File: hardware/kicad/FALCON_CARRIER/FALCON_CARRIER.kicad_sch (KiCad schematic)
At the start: 49 parts, among them J1 POWER_INPUT, J10 LEAK_SENSOR_TBD, J11 FAN1_MOLEX_470531000, J12 SERVICE_I2C, J13 FAN2_MOLEX_470531000, J2 BAR02_I2C, J3 GPS_UART, J4 INA260_BAT_LOGIC, J5 INA260_SOLAR_0X41, J6 MCP9808_0X18, J7 ANEMOMETER, J8 WIND_VANE, J9 DS18B20_OPTION, Q1 2N7002_FAN1_PWM, Q2 2N7002_FAN2_PWM, U1 REGULATOR_3V3_TBD, U2 ESP32_DEVKITC_V4_WROOM32E, U3 BNO085_SPI, U4 ADS1115_0X48, U6 EFUSE_TPS25947_TBD

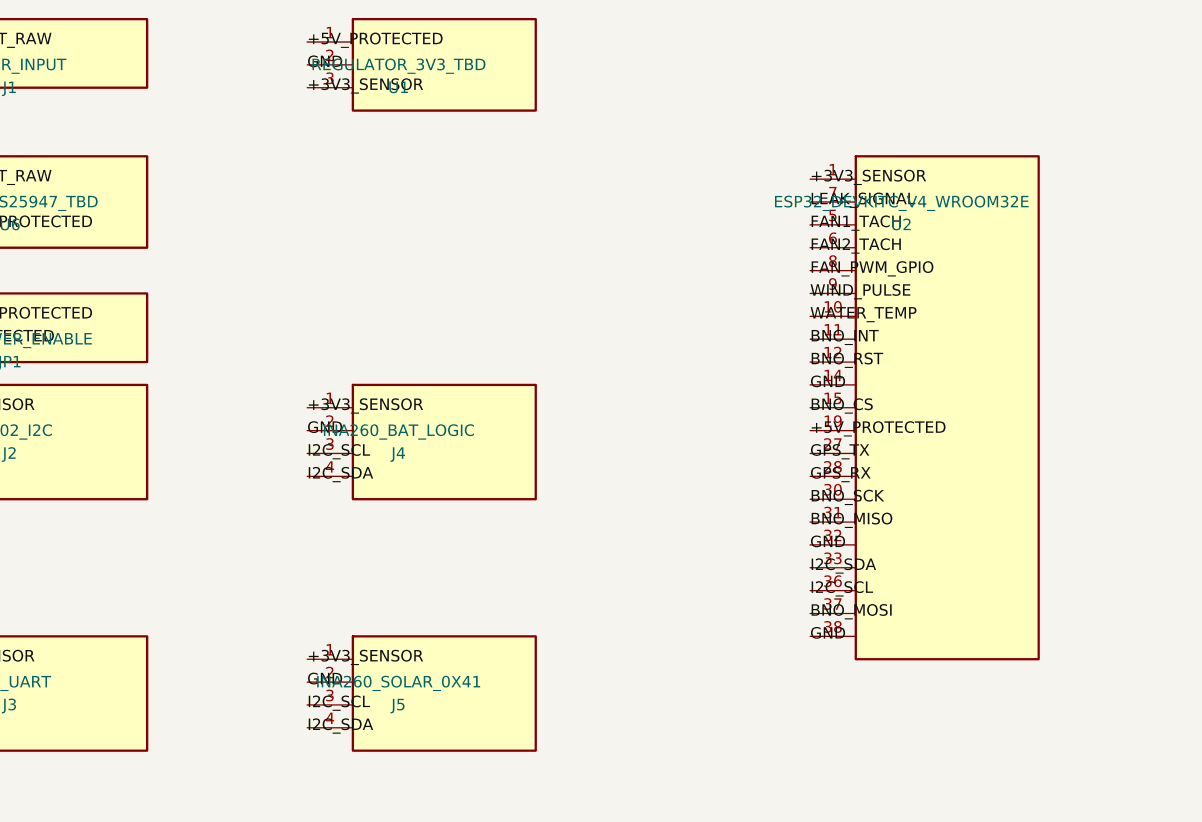
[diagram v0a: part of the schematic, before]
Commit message: Implement dedicated 3V3 sensor regulator
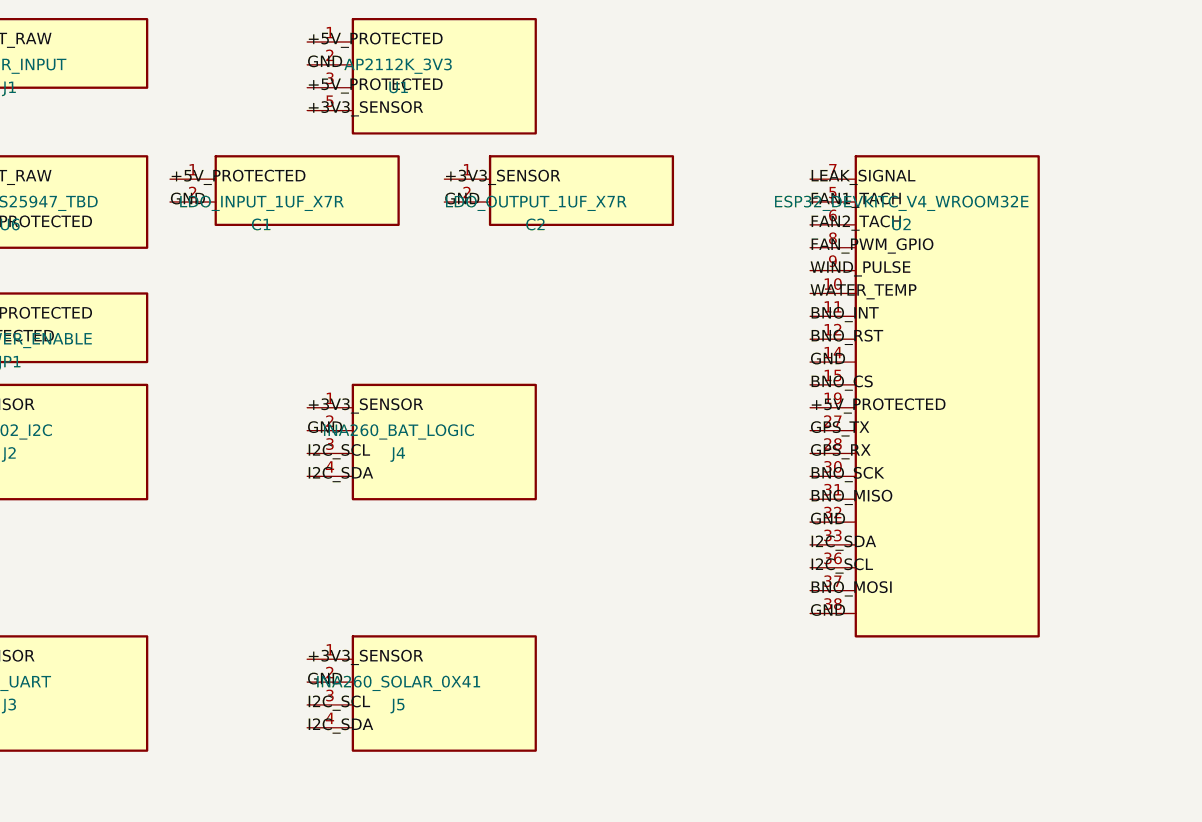
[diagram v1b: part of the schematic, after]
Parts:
- added C1: LDO_INPUT_1UF_X7R, symbol FALCON:LDO_INPUT_1UF_X7R
- added C2: LDO_OUTPUT_1UF_X7R, symbol FALCON:LDO_OUTPUT_1UF_X7R
- U1: value REGULATOR_3V3_TBD -> AP2112K_3V3; symbol FALCON:REGULATOR_3V3_TBD -> FALCON:AP2112K_3V3
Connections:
- net +3V3_SENSOR: now also U1.5 (+3V3_SENSOR), C2.1 (+3V3_SENSOR); no longer U1.3 (+3V3_SENSOR), U2.1 (+3V3_SENSOR)
- net +5V_PROTECTED: now also U1.3 (+5V_PROTECTED), C1.1 (+5V_PROTECTED)
- net GND: now also C1.2 (GND), C2.2 (GND)
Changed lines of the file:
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@@
   (label "GND" (at 88.90 38.10 0)
     (effects (font (size 1.27 1.27))))
-  (label "+3V3_SENSOR" (at 88.90 40.64 0)
-    (effects (font (size 1.27 1.27))))
-  (label "+3V3_SENSOR" (at 144.78 50.80 0)
-    (effects (font (size 1.27 1.27))))
-  (label "LEAK_SIGNAL" (at 144.78 53.34 0)
-    (effects (font (size 1.27 1.27))))
-  (label "FAN1_TACH" (at 144.78 55.88 0)
-    (effects (font (size 1.27 1.27))))
-  (label "FAN2_TACH" (at 144.78 58.42 0)
-    (effects (font (size 1.27 1.27))))
-  (label "FAN_PWM_GPIO" (at 144.78 60.96 0)
-    (effects (font (size 1.27 1.27))))
-  (label "WIND_PULSE" (at 144.78 63.50 0)
-    (effects (font (size 1.27 1.27))))
-  (label "WATER_TEMP" (at 144.78 66.04 0)
-    (effects (font (size 1.27 1.27))))
-  (label "BNO_INT" (at 144.78 68.58 0)
-    (effects (font (size 1.27 1.27))))
-  (label "BNO_RST" (at 144.78 71.12 0)
-    (effects (font (size 1.27 1.27))))
-  (label "GND" (at 144.78 73.66 0)
-    (effects (font (size 1.27 1.27))))
-  (label "BNO_CS" (at 144.78 76.20 0)
-    (effects (font (size 1.27 1.27))))
-  (label "+5V_PROTECTED" (at 144.78 78.74 0)
-    (effects (font (size 1.27 1.27))))
-  (label "GPS_TX" (at 144.78 81.28 0)
-    (effects (font (size 1.27 1.27))))
-  (label "GPS_RX" (at 144.78 83.82 0)
-    (effects (font (size 1.27 1.27))))
-  (label "BNO_SCK" (at 144.78 86.36 0)
-    (effects (font (size 1.27 1.27))))
-  (label "BNO_MISO" (at 144.78 88.90 0)
-    (effects (font (size 1.27 1.27))))
-  (label "GND" (at 144.78 91.44 0)
-    (effects (font (size 1.27 1.27))))
-  (label "I2C_SDA" (at 144.78 93.98 0)
-    (effects (font (size 1.27 1.27))))
-  (label "I2C_SCL" (at 144.78 96.52 0)
-    (effects (font (size 1.27 1.27))))
-  (label "BNO_MOSI" (at 144.78 99.06 0)
-    (effects (font (size 1.27 1.27))))
-  (label "GND" (at 144.78 101.60 0)
+  (label "+5V_PROTECTED" (at 88.90 40.64 0)
+    (effects (font (size 1.27 1.27))))
+  (label "+3V3_SENSOR" (at 88.90 43.18 0)
+    (effects (font (size 1.27 1.27))))
+  (label "+5V_PROTECTED" (at 73.66 50.80 0)
+    (effects (font (size 1.27 1.27))))
+  (label "GND" (at 73.66 53.34 0)
+    (effects (font (size 1.27 1.27))))
+  (label "+3V3_SENSOR" (at 104.14 50.80 0)
+    (effects (font (size 1.27 1.27))))
+  (label "GND" (at 104.14 53.34 0)
+    (effects (font (size 1.27 1.27))))
+  (label "LEAK_SIGNAL" (at 144.78 50.80 0)
+    (effects (font (size 1.27 1.27))))
+  (label "FAN1_TACH" (at 144.78 53.34 0)
+    (effects (font (size 1.27 1.27))))
+  (label "FAN2_TACH" (at 144.78 55.88 0)
+    (effects (font (size 1.27 1.27))))
+  (label "FAN_PWM_GPIO" (at 144.78 58.42 0)
+    (effects (font (size 1.27 1.27))))
+  (label "WIND_PULSE" (at 144.78 60.96 0)
+    (effects (font (size 1.27 1.27))))
+  (label "WATER_TEMP" (at 144.78 63.50 0)
+    (effects (font (size 1.27 1.27))))
+  (label "BNO_INT" (at 144.78 66.04 0)
+    (effects (font (size 1.27 1.27))))
+  (label "BNO_RST" (at 144.78 68.58 0)
+    (effects (font (size 1.27 1.27))))
+  (label "GND" (at 144.78 71.12 0)
+    (effects (font (size 1.27 1.27))))
+  (label "BNO_CS" (at 144.78 73.66 0)
+    (effects (font (size 1.27 1.27))))
+  (label "+5V_PROTECTED" (at 144.78 76.20 0)
+    (effects (font (size 1.27 1.27))))
+  (label "GPS_TX" (at 144.78 78.74 0)
+    (effects (font (size 1.27 1.27))))
+  (label "GPS_RX" (at 144.78 81.28 0)
+    (effects (font (size 1.27 1.27))))
+  (label "BNO_SCK" (at 144.78 83.82 0)
+    (effects (font (size 1.27 1.27))))
+  (label "BNO_MISO" (at 144.78 86.36 0)
+    (effects (font (size 1.27 1.27))))
+  (label "GND" (at 144.78 88.90 0)
+    (effects (font (size 1.27 1.27))))
+  (label "I2C_SDA" (at 144.78 91.44 0)
+    (effects (font (size 1.27 1.27))))
+  (label "I2C_SCL" (at 144.78 93.98 0)
+    (effects (font (size 1.27 1.27))))
+  (label "BNO_MOSI" (at 144.78 96.52 0)
+    (effects (font (size 1.27 1.27))))
+  (label "GND" (at 144.78 99.06 0)
     (effects (font (size 1.27 1.27))))
   (label "+3V3_SENSOR" (at 210.82 45.72 0)
@@
   )
   (symbol
-    (lib_id "FALCON:REGULATOR_3V3_TBD") (at 99.06 35.56 0) (unit 1)
+    (lib_id "FALCON:AP2112K_3V3") (at 99.06 35.56 0) (unit 1)
     (exclude_from_sim no) (in_bom yes) (on_board yes) (dnp no)
     (property "Reference" "U1" (at 99.06 40.64 0) (effects (font (size 1.27 1.27))))
-    (property "Value" "REGULATOR_3V3_TBD" (at 99.06 38.10 0) (effects (font (size 1.27 1.27))))
+    (property "Value" "AP2112K_3V3" (at 99.06 38.10 0) (effects (font (size 1.27 1.27))))
     (property "Footprint" "" (at 99.06 35.56 0) (effects (font (size 1.27 1.27)) (hide yes)))
     (property "Datasheet" "" (at 99.06 35.56 0) (effects (font (size 1.27 1.27)) (hide yes)))
@@
     (pin "2")
     (pin "3")
+    (pin "5")
     (instances (project "FALCON_CARRIER"
       (path "/8f84bda8-4a60-4fb6-9df1-43d0356dc759" (reference "U1") (unit 1))))
+  )
+  (symbol
+    (lib_id "FALCON:LDO_INPUT_1UF_X7R") (at 83.82 50.80 0) (unit 1)
+    (exclude_from_sim no) (in_bom yes) (on_board yes) (dnp no)
+    (property "Reference" "C1" (at 83.82 55.88 0) (effects (font (size 1.27 1.27))))
+    (property "Value" "LDO_INPUT_1UF_X7R" (at 83.82 53.34 0) (effects (font (size 1.27 1.27))))
+    (property "Footprint" "" (at 83.82 50.80 0) (effects (font (size 1.27 1.27)) (hide yes)))
+    (property "Datasheet" "" (at 83.82 50.80 0) (effects (font (size 1.27 1.27)) (hide yes)))
+    (property "Description" "FALCON carrier placeholder; footprint TBD" (at 83.82 50.80 0) (effects (font (size 1.27 1.27)) (hide yes)))
+    (pin "1")
+    (pin "2")
+    (instances (project "FALCON_CARRIER"
+      (path "/8f84bda8-4a60-4fb6-9df1-43d0356dc759" (reference "C1") (unit 1))))
+  )
+  (symbol
+    (lib_id "FALCON:LDO_OUTPUT_1UF_X7R") (at 114.30 50.80 0) (unit 1)
+    (exclude_from_sim no) (in_bom yes) (on_board yes) (dnp no)
+    (property "Reference" "C2" (at 114.30 55.88 0) (effects (font (size 1.27 1.27))))
+    (property "Value" "LDO_OUTPUT_1UF_X7R" (at 114.30 53.34 0) (effects (font (size 1.27 1.27))))
+    (property "Footprint" "" (at 114.30 50.80 0) (effects (font (size 1.27 1.27)) (hide yes)))
+    (property "Datasheet" "" (at 114.30 50.80 0) (effects (font (size 1.27 1.27)) (hide yes)))
+    (property "Description" "FALCON carrier placeholder; footprint TBD" (at 114.30 50.80 0) (effects (font (size 1.27 1.27)) (hide yes)))
+    (pin "1")
+    (pin "2")
+    (instances (project "FALCON_CARRIER"
+      (path "/8f84bda8-4a60-4fb6-9df1-43d0356dc759" (reference "C2") (unit 1))))
   )
   (symbol
@@
     (property "Datasheet" "" (at 154.94 50.80 0) (effects (font (size 1.27 1.27)) (hide yes)))
     (property "Description" "FALCON carrier placeholder; footprint TBD" (at 154.94 50.80 0) (effects (font (size 1.27 1.27)) (hide yes)))
-    (pin "1")
     (pin "7")
     (pin "5")

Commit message: Redesign FALCON carrier schematic blocks
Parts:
- removed C1: LDO_INPUT_1UF_X7R, symbol FALCON:LDO_INPUT_1UF_X7R
- removed C2: LDO_OUTPUT_1UF_X7R, symbol FALCON:LDO_OUTPUT_1UF_X7R
- removed J1: POWER_INPUT, symbol FALCON:POWER_INPUT
- removed J10: LEAK_SENSOR_TBD, symbol FALCON:LEAK_SENSOR_TBD
- removed J11: FAN1_MOLEX_470531000, symbol FALCON:FAN1_MOLEX_470531000
- removed J12: SERVICE_I2C, symbol FALCON:SERVICE_I2C
- removed J13: FAN2_MOLEX_470531000, symbol FALCON:FAN2_MOLEX_470531000
- removed J2: BAR02_I2C, symbol FALCON:BAR02_I2C
- removed J3: GPS_UART, symbol FALCON:GPS_UART
- removed J4: INA260_BAT_LOGIC, symbol FALCON:INA260_BAT_LOGIC
- removed J5: INA260_SOLAR_0X41, symbol FALCON:INA260_SOLAR_0X41
- removed J6: MCP9808_0X18, symbol FALCON:MCP9808_0X18
- removed J7: ANEMOMETER, symbol FALCON:ANEMOMETER
- removed J8: WIND_VANE, symbol FALCON:WIND_VANE
- removed J9: DS18B20_OPTION, symbol FALCON:DS18B20_OPTION
- removed JP1: EXT_POWER_ENABLE, symbol FALCON:EXT_POWER_ENABLE
- removed Q1: 2N7002_FAN1_PWM, symbol FALCON:2N7002_FAN1_PWM
- removed Q2: 2N7002_FAN2_PWM, symbol FALCON:2N7002_FAN2_PWM
- removed R1: PULLUP_10K, symbol FALCON:PULLUP_10K
- removed R2: PULLUP_4K7, symbol FALCON:PULLUP_4K7
- removed R3: FAN1_GATE_100R, symbol FALCON:FAN1_GATE_100R
- removed R4: FAN2_GATE_100R, symbol FALCON:FAN2_GATE_100R
- removed R5: FAN1_GATE_PULLDOWN_100K, symbol FALCON:FAN1_GATE_PULLDOWN_100K
- removed R6: FAN2_GATE_PULLDOWN_100K, symbol FALCON:FAN2_GATE_PULLDOWN_100K
- removed R7: FAN1_TACH_PULLUP_10K, symbol FALCON:FAN1_TACH_PULLUP_10K
- removed R8: FAN2_TACH_PULLUP_10K, symbol FALCON:FAN2_TACH_PULLUP_10K
- removed TP1, TP10, TP11, TP12, TP13, TP14, TP15, TP16, TP17, TP18, TP19, TP2, TP20, TP3, TP4, TP5, TP6, TP7, TP8, TP9: TEST_POINT, symbol FALCON:TEST_POINT
- removed U3: BNO085_SPI, symbol FALCON:BNO085_SPI
- removed U4: ADS1115_0X48, symbol FALCON:ADS1115_0X48
- removed U6: EFUSE_TPS25947_TBD, symbol FALCON:EFUSE_TPS25947_TBD
- added C1: 1UF_LDO_IN, Capacitor_SMD:C_0603_1608Metric, symbol FALCON:1UF_LDO_IN
- added C2: 1UF_LDO_OUT, Capacitor_SMD:C_0603_1608Metric, symbol FALCON:1UF_LDO_OUT
- added C3: 10UF_25V_INPUT, Capacitor_SMD:C_0603_1608Metric, symbol FALCON:10UF_25V_INPUT
- added C4: 47UF_10V_OUTPUT, Capacitor_SMD:C_1210_3225Metric, symbol FALCON:47UF_10V_OUTPUT
- added C5: 100NF_5V_DECOUPLING, Capacitor_SMD:C_0603_1608Metric, symbol FALCON:100NF_5V_DECOUPLING
- added C6: 10UF_5V_BULK, Capacitor_SMD:C_0805_2012Metric, symbol FALCON:10UF_5V_BULK
- added D1: SMBJ18A_TVS, Diode_SMD:D_SMA, symbol FALCON:SMBJ18A_TVS
- added D2: 5V_POWER_LED, LED_SMD:LED_0603_1608Metric, symbol FALCON:5V_POWER_LED
- added D3: 3V3_POWER_LED, LED_SMD:LED_0603_1608Metric, symbol FALCON:3V3_POWER_LED
- added D4: STATUS_LED, LED_SMD:LED_0603_1608Metric, symbol FALCON:STATUS_LED
- added F1: FUSE_3A_DC_TBD, Fuse:Fuse_1206_3216Metric, symbol FALCON:FUSE_3A_DC_TBD
- added F2: USB_POLYFUSE_1A, Fuse:Fuse_1206_3216Metric, symbol FALCON:USB_POLYFUSE_1A
- added J10: LEAK_SENSOR_INTERFACE, Connector_PinHeader_2.54mm:PinHeader_1x03_P2.54mm_Vertical, symbol FALCON:LEAK_SENSOR_INTERFACE
- added J14: SOLAR_INPUT_TO_EXTERNAL_MPPT, Connector_JST:JST_VH_B2P-VH-B_1x02_P3.96mm_Vertical, symbol FALCON:SOLAR_INPUT_TO_EXTERNAL_MPPT
- added J15: BATTERY_INPUT_12V8, Connector_JST:JST_VH_B2P-VH-B_1x02_P3.96mm_Vertical, symbol FALCON:BATTERY_INPUT_12V8
- added J16: USB_C_SERVICE_POWER, Connector_USB:USB_C_Receptacle_USB2.0_16P, symbol FALCON:USB_C_SERVICE_POWER
- added J2: PRESSURE_BAR02_I2C, Connector_PinHeader_2.54mm:PinHeader_1x04_P2.54mm_Vertical, symbol FALCON:PRESSURE_BAR02_I2C
- added J20: EXTERNAL_EDGE_UART, Connector_PinHeader_2.54mm:PinHeader_1x04_P2.54mm_Vertical, symbol FALCON:EXTERNAL_EDGE_UART
- added J21: ESP32_PROGRAM_HEADER, Connector_PinHeader_2.54mm:PinHeader_1x06_P2.54mm_Vertical, symbol FALCON:ESP32_PROGRAM_HEADER
- added J22: FUTURE_I2C_HEADER, Connector_PinHeader_2.54mm:PinHeader_1x04_P2.54mm_Vertical, symbol FALCON:FUTURE_I2C_HEADER
- added J23: EXPANSION_HEADER, Connector_PinHeader_2.54mm:PinHeader_1x06_P2.54mm_Vertical, symbol FALCON:EXPANSION_HEADER
- added J3: GPS_UART_MODULE, Connector_PinHeader_2.54mm:PinHeader_1x04_P2.54mm_Vertical, symbol FALCON:GPS_UART_MODULE
- added J4: BATTERY_MONITOR_INA260, Connector_PinHeader_2.54mm:PinHeader_1x04_P2.54mm_Vertical, symbol FALCON:BATTERY_MONITOR_INA260
- added J5: SOLAR_MONITOR_INA260, Connector_PinHeader_2.54mm:PinHeader_1x04_P2.54mm_Vertical, symbol FALCON:SOLAR_MONITOR_INA260
- added J6: ENCLOSURE_TEMP_MCP9808, Connector_PinHeader_2.54mm:PinHeader_1x04_P2.54mm_Vertical, symbol FALCON:ENCLOSURE_TEMP_MCP9808
- added J7: WIND_SPEED_SENSOR, Connector_PinHeader_2.54mm:PinHeader_1x03_P2.54mm_Vertical, symbol FALCON:WIND_SPEED_SENSOR
- added J8: WIND_DIRECTION_SENSOR, Connector_PinHeader_2.54mm:PinHeader_1x03_P2.54mm_Vertical, symbol FALCON:WIND_DIRECTION_SENSOR
- added J9: TEMPERATURE_DS18B20, Connector_PinHeader_2.54mm:PinHeader_1x03_P2.54mm_Vertical, symbol FALCON:TEMPERATURE_DS18B20
- added JP1: USB_SERVICE_ENABLE, Connector_PinHeader_2.54mm:PinHeader_1x02_P2.54mm_Vertical, symbol FALCON:USB_SERVICE_ENABLE
- added Q3: REVERSE_POLARITY_PFET_30V, Package_TO_SOT_SMD:SOT-23, symbol FALCON:REVERSE_POLARITY_PFET_30V
- added R1: 4K7_I2C_SDA_PULLUP, Resistor_SMD:R_0603_1608Metric, symbol FALCON:4K7_I2C_SDA_PULLUP
- added R10: 1K_LED3, Resistor_SMD:R_0603_1608Metric, symbol FALCON:1K_LED3
- added R11: 5K1_CC1, Resistor_SMD:R_0603_1608Metric, symbol FALCON:5K1_CC1
- added R12: 5K1_CC2, Resistor_SMD:R_0603_1608Metric, symbol FALCON:5K1_CC2
- added R13: 10K_EN_PULLUP, Resistor_SMD:R_0603_1608Metric, symbol FALCON:10K_EN_PULLUP
- added R14: 10K_BOOT_PULLUP, Resistor_SMD:R_0603_1608Metric, symbol FALCON:10K_BOOT_PULLUP
- added R15: 330R_STATUS, Resistor_SMD:R_0603_1608Metric, symbol FALCON:330R_STATUS
- added R2: 4K7_I2C_SCL_PULLUP, Resistor_SMD:R_0603_1608Metric, symbol FALCON:4K7_I2C_SCL_PULLUP
- added R3: 10K_WIND_PULLUP, Resistor_SMD:R_0603_1608Metric, symbol FALCON:10K_WIND_PULLUP
- added R4: 4K7_ONEWIRE_PULLUP, Resistor_SMD:R_0603_1608Metric, symbol FALCON:4K7_ONEWIRE_PULLUP
- added R9: 1K_LED5, Resistor_SMD:R_0603_1608Metric, symbol FALCON:1K_LED5
- added SW1: MAIN_POWER_SWITCH, Button_Switch_THT:SW_CW_G1_SPST, symbol FALCON:MAIN_POWER_SWITCH
- added SW2: RESET_BUTTON, Button_Switch_SMD:SW_SPST_TL3342, symbol FALCON:RESET_BUTTON
- added SW3: BOOT_BUTTON, Button_Switch_SMD:SW_SPST_TL3342, symbol FALCON:BOOT_BUTTON
- added TP1: TESTPOINT_P3V3, TestPoint:TestPoint_Plated_Hole_D1.0mm, symbol FALCON:TESTPOINT_P3V3
- added TP2: TESTPOINT_P5V, TestPoint:TestPoint_Plated_Hole_D1.0mm, symbol FALCON:TESTPOINT_P5V
- added TP3: TESTPOINT_PVBAT, TestPoint:TestPoint_Plated_Hole_D1.0mm, symbol FALCON:TESTPOINT_PVBAT
- added TP4: TESTPOINT_UART_TX, TestPoint:TestPoint_Plated_Hole_D1.0mm, symbol FALCON:TESTPOINT_UART_TX
- added TP5: TESTPOINT_UART_RX, TestPoint:TestPoint_Plated_Hole_D1.0mm, symbol FALCON:TESTPOINT_UART_RX
- added TP6: TESTPOINT_SDA, TestPoint:TestPoint_Plated_Hole_D1.0mm, symbol FALCON:TESTPOINT_SDA
- added TP7: TESTPOINT_SCL, TestPoint:TestPoint_Plated_Hole_D1.0mm, symbol FALCON:TESTPOINT_SCL
- added TP8: TESTPOINT_GND, TestPoint:TestPoint_Plated_Hole_D1.0mm, symbol FALCON:TESTPOINT_GND
- added U3: BNO085_IMU_SPI, Connector_PinHeader_2.54mm:PinHeader_1x06_P2.54mm_Vertical, symbol FALCON:BNO085_IMU_SPI
- added U4: WIND_DIRECTION_ADS1115, Connector_PinHeader_2.54mm:PinHeader_1x06_P2.54mm_Vertical, symbol FALCON:WIND_DIRECTION_ADS1115
- added U7: 5V_2A_BUCK_MODULE, Connector_PinHeader_2.54mm:PinHeader_1x04_P2.54mm_Vertical, symbol FALCON:5V_2A_BUCK_MODULE
- U1: footprint (none) -> Package_TO_SOT_SMD:SOT-23-5
- U2: footprint (none) -> ${KIPRJMOD}/vendor/Espressif.pretty/ESP32-DevKitC.kicad_mod
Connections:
- net BNO_CS: now also U3.6 (CS)
- net BNO_INT: now also U3.7 (INT)
- net BNO_MISO: now also U3.4 (MISO)
- net BNO_MOSI: now also U3.5 (MOSI)
- net BNO_RST: now also U3.8 (RST)
- net BNO_SCK: now also U3.3 (SCK)
- net GND: now also C1.2 (-), C2.2 (-), C3.2 (-), C4.2 (-), C5.2 (-), C6.2 (-), D1.2 (A), D4.2 (K), J10.3 (GND), J14.2 (SOLAR-), J15.2 (-), J16.2 (GND), J2.4 (GND), J20.2 (GND), J21.2 (GND), J22.2 (GND), J23.3 (GND), J3.2 (GND), J4.2 (GND), J5.2 (GND), J6.4 (GND), J7.3 (GND), J8.3 (GND), J9.3 (GND), Q3.2 (G), R10.2, R11.2, R12.2, R9.2, SW2.2 (GND), SW3.2 (GND), TP8.1 (GND), U3.2 (GND), U4.2 (GND), U7.2 (GND)
- net GPS_RX: now also J3.4 (GPS_RX)
- net GPS_TX: now also J3.3 (GPS_TX)
- net I2C_SCL: now also J2.2 (SCL), J22.4 (SCL), J23.6 (SCL), J4.3 (SCL), J5.3 (SCL), J6.2 (SCL), R2.2 (SCL), TP7.1 (I2C_SCL), U4.3 (SCL)
- net I2C_SDA: now also J2.3 (SDA), J22.3 (SDA), J23.5 (SDA), J4.4 (SDA), J5.4 (SDA), J6.3 (SDA), R1.2 (SDA), TP6.1 (I2C_SDA), U4.4 (SDA)
- net LEAK_SIGNAL: now also J10.2 (SIGNAL)
- net WATER_TEMP: now also J9.2 (DATA), R4.2 (DATA)
- net +3V3_SENSOR renamed +3V3
- net +3V3: now also C2.1 (+), D3.1 (A), J10.1 (3V3), J2.1 (3V3), J21.1 (3V3), J22.1 (3V3), J23.1 (3V3), J3.1 (3V3), J4.1 (3V3), J5.1 (3V3), J6.1 (3V3), J7.1 (3V3), J8.1 (3V3), J9.1 (3V3), R1.1 (3V3), R13.1, R14.1, R2.1 (3V3), R3.1 (3V3), R4.1 (3V3), TP1.1 (+3V3), U3.1 (3V3), U4.1 (3V3)
- net +5V_PROTECTED renamed +5V
- net +5V: now also C1.1 (+), C4.1 (+), C5.1 (+), C6.1 (+), D2.1 (A), J20.1 (5V_SERVICE), J23.2 (5V), JP1.2 (RAIL), TP2.1 (+5V), U7.3 (VOUT)
- net WIND_PULSE renamed WIND_SPEED
- net WIND_SPEED: now also J7.2 (PULSE), R3.2 (PULSE)
- new net +VBAT: Q3.3 (D), SW1.1 (IN), TP3.1 (+VBAT)
- new net +VBAT_FUSED: D1.1 (K), F1.2 (OUT), Q3.1 (S)
- new net +VBAT_RAW: F1.1 (IN), J15.1 (+)
- new net +VBAT_SW: C3.1 (+), SW1.2 (OUT), U7.1 (VIN), U7.4 (EN)
- new net BOOT_GPIO0: J21.6 (BOOT), R14.2, SW3.1 (GPIO0), U2.25 (GPIO0)
- new net ESP_EN: J21.5 (EN), R13.2, SW2.1 (EN), U2.3 (EN)
- new net EXP_GPIO4: J23.4 (GPIO4), U2.26 (GPIO4)
- new net LED3_K: D3.2 (K), R10.1
- new net LED5_K: D2.2 (K), R9.1
- new net SOLAR_RAW: J14.1 (SOLAR+)
- new net STATUS_LED: R15.1 (GPIO), U2.24 (GPIO2)
- new net STATUS_LED_A: D4.1 (A), R15.2 (LED)
- new net UART_RX: J20.4 (ESP_RX), J21.4 (RX0), TP5.1 (UART_RX), U2.34 (RX0)
- new net UART_TX: J20.3 (ESP_TX), J21.3 (TX0), TP4.1 (UART_TX), U2.35 (TX0)
- new net USB_5V_FUSED: F2.2 (OUT), JP1.1 (USB)
- new net USB_CC1: J16.3 (CC1), R11.1
- new net USB_CC2: J16.4 (CC2), R12.1
- new net USB_DMINUS_NC: J16.6 (D-_NC)
- new net USB_DPLUS_NC: J16.5 (D+_NC)
- new net USB_VBUS: F2.1 (IN), J16.1 (VBUS)
- new net WIND_DIR: J8.2 (ADC), U4.5 (A0)
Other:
- note added: "1. POWER MANAGEMENT"
- note added: "2. ESP32 CONTROLLER"
- note added: "3. SENSOR INTERFACES"
- note added: "4. COMMUNICATION"
- note added: "5. DEBUG & EXPANSION"
- note added: "EXTERNAL EDGE COMPUTER IS SEPARATELY POWERED; UART HEADER J20 ONLY; NOT ON THIS PCB"
- note added: "POWER → ESP32 → SENSORS → COMMUNICATION"
- note added: "SOLAR PANEL → EXTERNAL LiFePO4 MPPT → BATTERY. NEVER CONNECT PANEL DIRECTLY TO BATTERY."
- note added: "USB-C IS SERVICE POWER ONLY. ISOLATE BATTERY BUCK BEFORE FITTING JP1."
- title: FALCON-01 LOW-VOLTAGE CARRIER -> PROJECT FALCON — ESP32 SENSOR CARRIER
